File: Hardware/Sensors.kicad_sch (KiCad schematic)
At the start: 29 parts, among them Q7 BCR116, U5 MS5611-01BA, U6 ICM-42688-P, U7 ADXL375BCCZ-RL7, U9 MAX-M10N

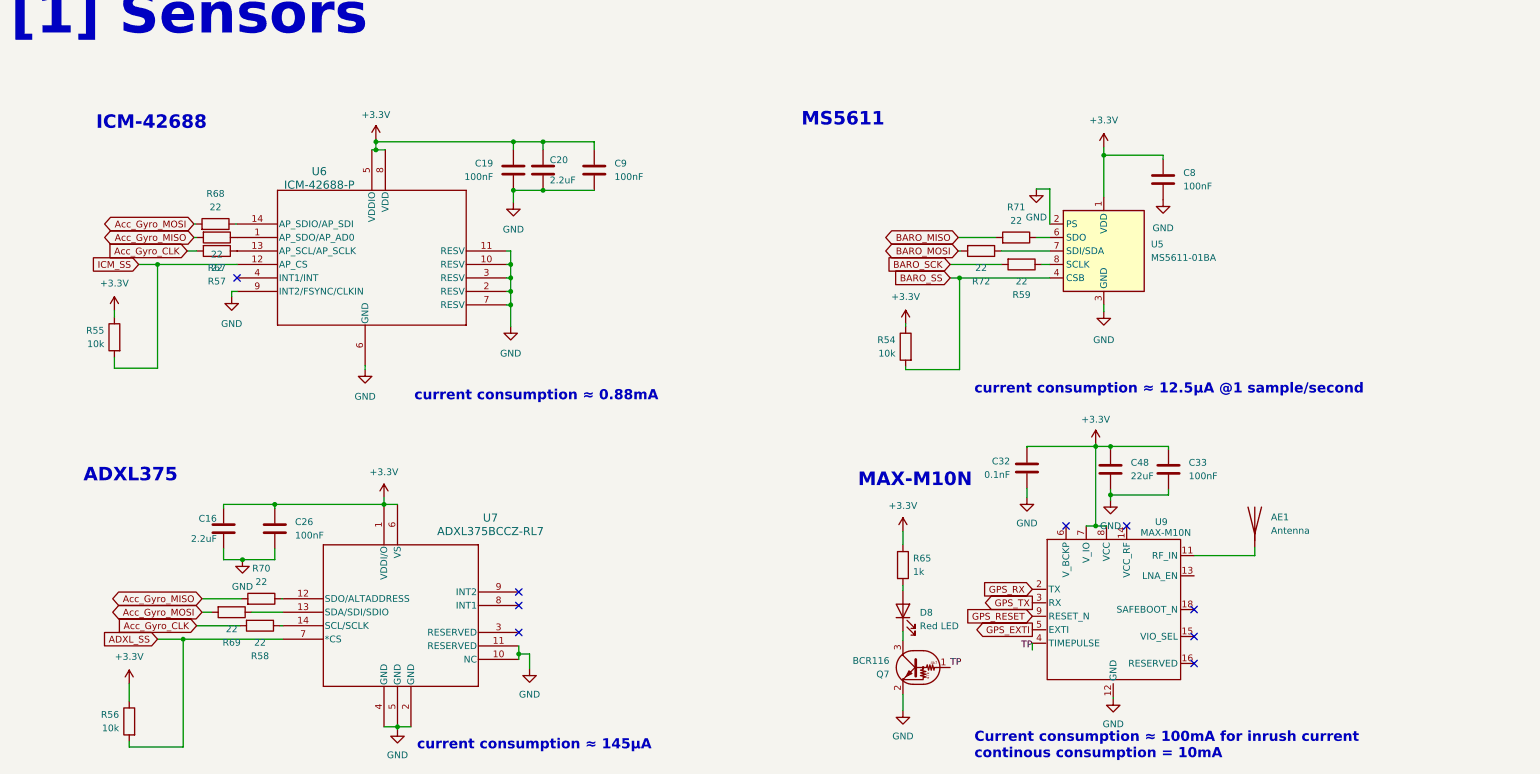
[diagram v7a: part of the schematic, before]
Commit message: Added Impedance matching calculations, finished buck converter calculations, finalized buzzer circuitry
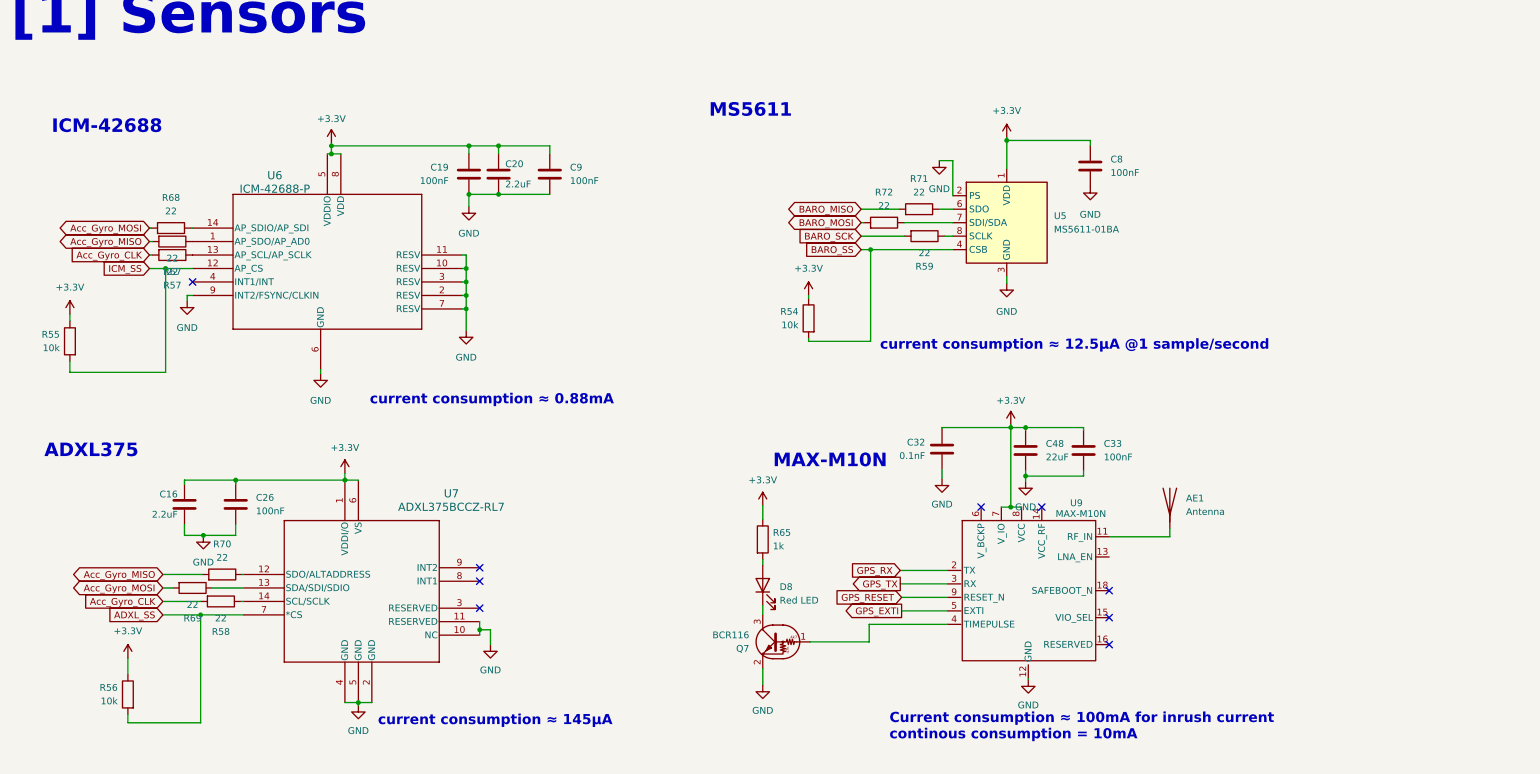
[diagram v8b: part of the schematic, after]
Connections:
- net TP: no longer names the net of Q7.1 (B), U9.4 (TIMEPULSE)
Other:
- moved on the sheet: AE1, C16, C19, C20, C26, C32, C33, C48, C8, C9, D8, Q7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
